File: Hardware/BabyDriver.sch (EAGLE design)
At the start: 34 parts, among them U1 L6470

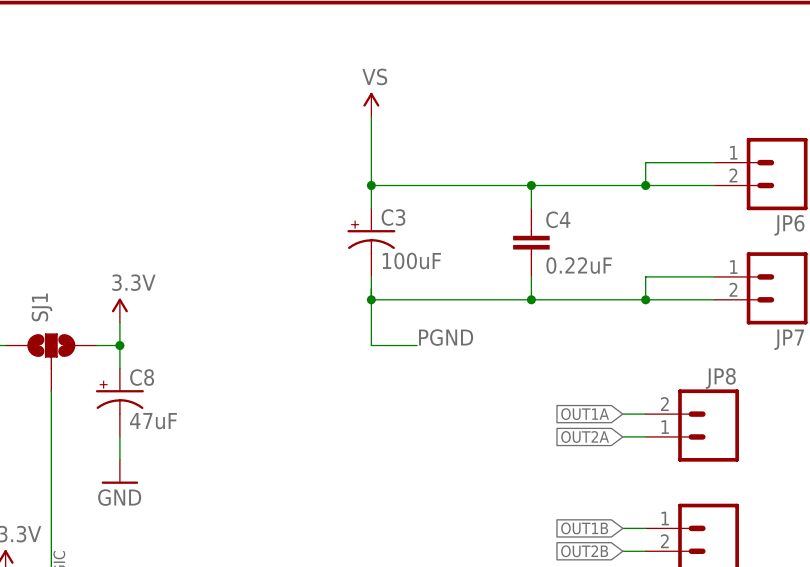
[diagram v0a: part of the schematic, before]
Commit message: v01 files, as sent to protos.
Mostly unchanged from initial commit; changed some part placements,
some silk.
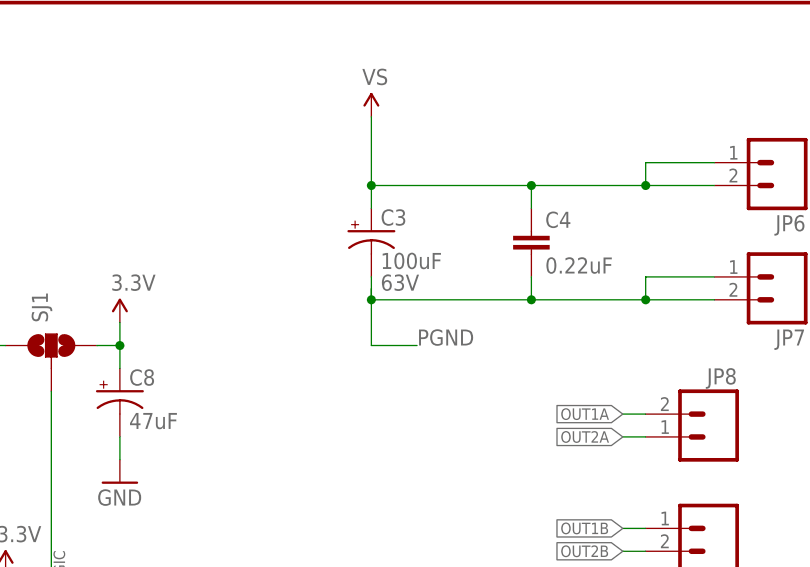
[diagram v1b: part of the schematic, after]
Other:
- note added: "63V"
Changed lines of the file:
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@@
 <text x="173.228" y="7.62" size="3.81" layer="94">Mike Hord</text>
 <text x="238.76" y="6.35" size="3.81" layer="94">01</text>
+<text x="194.056" y="153.416" size="1.778" layer="96">63V</text>
 </plain>
 <instances>

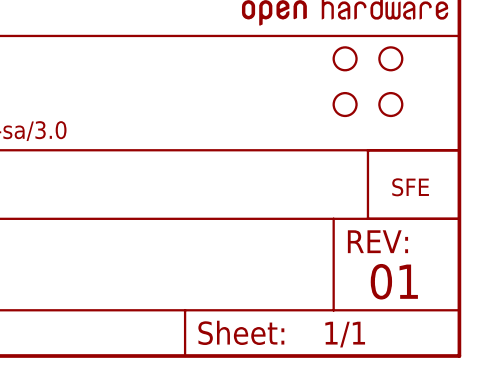
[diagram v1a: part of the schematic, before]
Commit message: Tidying up the example code some; that's still in process.
This is to update the hardware files to v02- shrink the board
a bit.
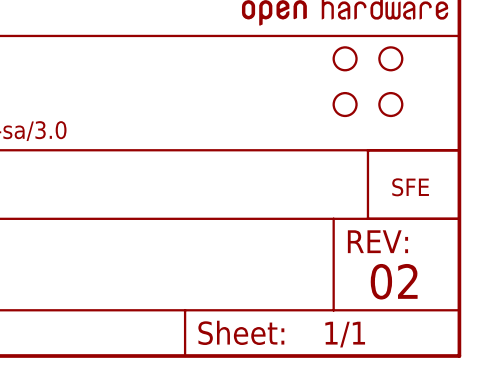
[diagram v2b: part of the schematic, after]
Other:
- note added: "02"
- note removed: "01"
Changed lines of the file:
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@@
 <plain>
 <text x="173.228" y="7.62" size="3.81" layer="94">Mike Hord</text>
-<text x="238.76" y="6.35" size="3.81" layer="94">01</text>
+<text x="238.76" y="6.35" size="3.81" layer="94">02</text>
 <text x="194.056" y="153.416" size="1.778" layer="96">63V</text>
 </plain>

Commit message: Fix mask on bottom layer
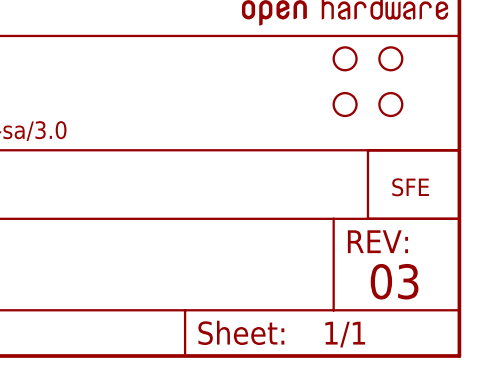
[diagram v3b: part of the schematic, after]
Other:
- note added: "03"
- note removed: "02"
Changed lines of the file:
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@@
 <plain>
 <text x="173.228" y="7.62" size="3.81" layer="94">Mike Hord</text>
-<text x="238.76" y="6.35" size="3.81" layer="94">02</text>
+<text x="238.76" y="6.35" size="3.81" layer="94">03</text>
 <text x="194.056" y="153.416" size="1.778" layer="96">63V</text>
 </plain>

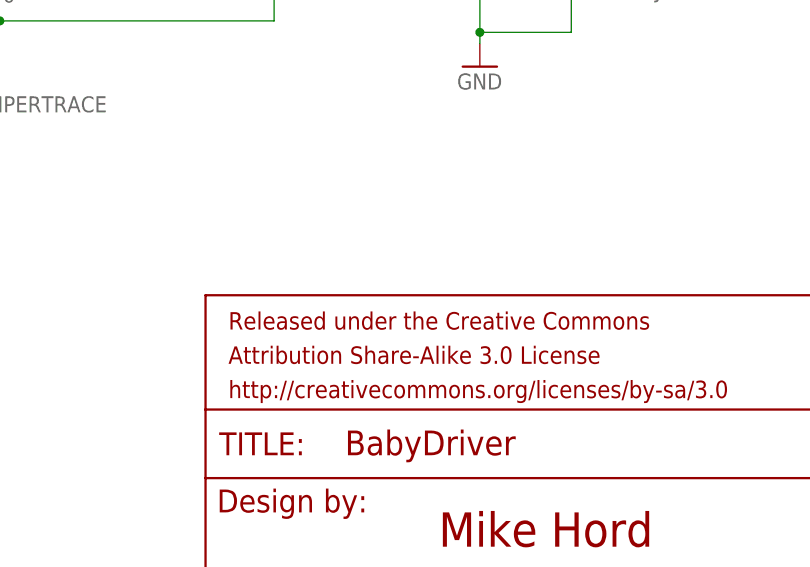
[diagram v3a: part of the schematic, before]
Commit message: Added four-layer warning to files.
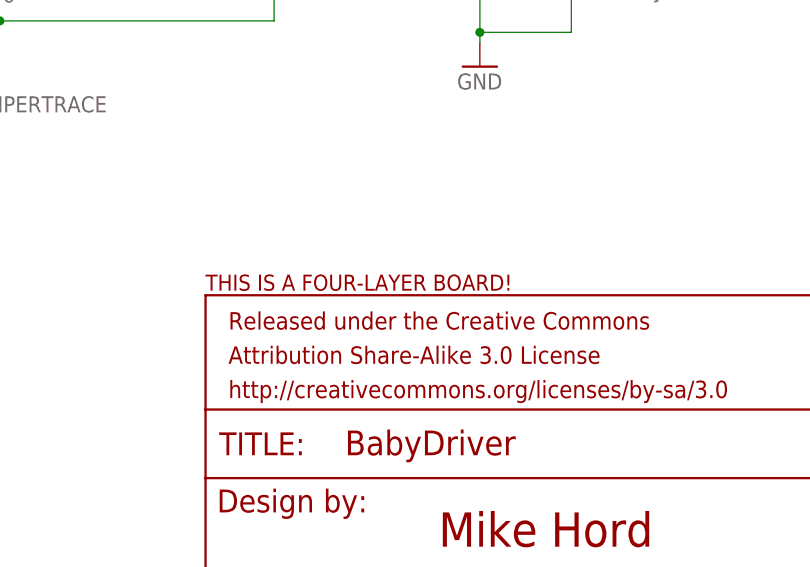
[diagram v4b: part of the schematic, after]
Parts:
- added U$4: FOUR_LAYER_WARNING, SparkFun-Aesthetics:FOUR_LAYER_WARNING
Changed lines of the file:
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@@
 <?xml version="1.0" encoding="utf-8"?>
 <!DOCTYPE eagle SYSTEM "eagle.dtd">
-<eagle version="6.3">
+<eagle version="6.4">
 <drawing>
 <settings>
@@
 <part name="GND12" library="SparkFun" deviceset="GND" device=""/>
 <part name="SJ2" library="SparkFun-Passives" deviceset="SOLDERJUMPER" device="TRACE"/>
+<part name="U$4" library="SparkFun-Aesthetics" deviceset="FOUR_LAYER_WARNING" device=""/>
 </parts>
 <sheets>
@@
 <instance part="GND12" gate="1" x="12.7" y="53.34"/>
 <instance part="SJ2" gate="1" x="114.3" y="60.96"/>
+<instance part="U$4" gate="G$1" x="147.32" y="36.068"/>
 </instances>
 <busses>
